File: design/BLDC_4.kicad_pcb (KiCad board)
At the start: 4 copper layers, 38.5 x 65 mm, 127 parts, among them K1 SERVO, P1 HALL/Encoder, P101 CANBUS, P2 SWD, P3 PWR_COMM, P4 IN+, P5 IN-, P6 MOTOR1, P7 MOTOR2, P9 MOTOR3, Q1 IRFS7530, Q2 IRFS7530, Q3 IRFS7530, Q4 IRFS7530, Q5 IRFS7530, Q6 IRFS7530, U1 STM32F40X_LQFP64, U2 TC2117, U3 DRV8302, U401 SN65HVD232, X1 MINI-USB-SHIELD-32005-201, X2 8MHz 10ppm

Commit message: Version 0.1 :godmode:
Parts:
- removed 1PIN (x2): P***, 1pin
- removed 1PIN (x2): P***, Connect:1pin
- removed C401, C41, C52: 2.2u, CRF1:SMD-0603_c
- removed C43, C44, C49: 10u,50V, CRF1:SMD-1206
- removed C51: 15u, 100v, w_smd_cap:c_2220
- removed G***: oshw_silkscreen-back_3mm, oshw_silkscreen-back_3mm
- removed K1: SERVO, CRF1:pinhead-1X03
- removed P101: CANBUS, JST conn:b4b-ph-kl
- removed P9: MOTOR3, CRF1:1PAD_4x5mm
- removed R103, R104: 22R, CRF1:SMD-0603_r
- removed R36, R46: 39k, CRF1:SMD-0603_r
- removed R37, R38, R48, R49, R50, R51: 100R, CRF1:SMD-0603_r
- removed R401: NI, CRF1:SMD-0603_r
- removed R402: 10k, CRF1:SMD-0603_r
- removed R42, R43: 4R7, CRF1:SMD-0603_r
- removed R53, R54: SHUNT, CRF1:WSLP2726
- removed U401: SN65HVD232, CRF1:SOIC-8-W
- removed X2: 8MHz 10ppm, CRF1:Crystal_5x3mm
- added J1: Conn_01x04, Connector_PinHeader_2.54mm:PinHeader_1x04_P2.54mm_Vertical, F.Cu at (164.5, 59.1)
- added R14: 4R7, Resistor_SMD:R_0603_1608Metric, F.Cu at (200.5, 87.0)
- added R15: 4R7, Resistor_SMD:R_0603_1608Metric, F.Cu at (200.5, 88.9)
- added R16: 39k, Resistor_SMD:R_0603_1608Metric, F.Cu at (200.7, 84.5)
- added R31: 2k2, Resistor_SMD:R_0603_1608Metric, F.Cu at (174.6, 90.2)
- C1: value 10u,50V -> 100n; footprint CRF1:SMD-1206 -> Capacitor_SMD:C_0603_1608Metric_Pad1.05x0.95mm_HandSolder
- C10, C11, C12, C23: value 2.2u -> 10u,50V; footprint CRF1:SMD-0603_c -> Capacitor_SMD:C_1206_3216Metric
- C13: value 2.2u -> 100n; footprint CRF1:SMD-0603_c -> Capacitor_SMD:C_0603_1608Metric_Pad1.05x0.95mm_HandSolder
- C14, C16: value 2.2u -> 220n; footprint CRF1:SMD-0603_c -> Capacitor_SMD:C_0603_1608Metric_Pad1.05x0.95mm_HandSolder; moved to F.Cu
- C15: value 15p -> 220n; footprint CRF1:SMD-0603_c -> Capacitor_SMD:C_0603_1608Metric_Pad1.05x0.95mm_HandSolder; moved to F.Cu
- C17, C18: value 2.2u -> 2.2n; footprint CRF1:SMD-0603_c -> Capacitor_SMD:C_0603_1608Metric_Pad1.05x0.95mm_HandSolder; moved to F.Cu
- C19: value 120p -> 2.2u; footprint CRF1:SMD-0603_c -> Capacitor_SMD:C_0603_1608Metric_Pad1.05x0.95mm_HandSolder
- C2, C3: value 100n -> 2.2u; footprint CRF1:SMD-0603_c -> Capacitor_SMD:C_0603_1608Metric_Pad1.05x0.95mm_HandSolder; moved to F.Cu
- C20: value 2.2u -> 100u; footprint CRF1:SMD-0603_c -> Capacitor_Tantalum_SMD:CP_EIA-3528-21_Kemet-B; moved to F.Cu
- C21: value 6.8n -> 10u,50V; footprint CRF1:SMD-0603_c -> Capacitor_SMD:C_1206_3216Metric
- C22: value 22n -> 100u; footprint CRF1:SMD-0603_c -> Capacitor_Tantalum_SMD:CP_EIA-3528-21_Kemet-B
- C24, C26: value 2.2u -> 10u,50V; footprint CRF1:SMD-0603_c -> Capacitor_SMD:C_1206_3216Metric; moved to F.Cu
- C25: value 100u -> 15u, 100v; footprint w_smd_cap:c_tant_B -> Capacitor_SMD:C_2220_5650Metric; moved to F.Cu
- C27: value 100n -> 10u,50V; footprint CRF1:SMD-0603_c -> Capacitor_SMD:C_1206_3216Metric
- C28: value 220n -> 15u,100V; footprint CRF1:SMD-0603_c -> Capacitor_SMD:C_2220_5650Metric
- C29: value 220n -> 15p; footprint CRF1:SMD-0603_c -> Capacitor_SMD:C_0603_1608Metric
- C30: value 220n -> 2.2u; footprint CRF1:SMD-0603_c -> Capacitor_SMD:C_0603_1608Metric
- C31: footprint CRF1:SMD-0603_c -> Capacitor_SMD:C_0603_1608Metric; moved to F.Cu
- C32: value 100n -> 2.2u; footprint CRF1:SMD-0603_c -> Capacitor_SMD:C_0603_1608Metric; moved to F.Cu
- C33: value 100u -> 100n; footprint w_smd_cap:c_tant_B -> Capacitor_SMD:C_0603_1608Metric; moved to F.Cu
- C34, C36: value 2.2n -> 2.2u; footprint CRF1:SMD-0603_c -> Capacitor_SMD:C_0603_1608Metric
- C35: value 2.2u -> 15p; footprint CRF1:SMD-0603_c -> Capacitor_SMD:C_0603_1608Metric
- C37: value 15u,100V -> 2.2u; footprint w_smd_cap:c_2220 -> Capacitor_SMD:C_0603_1608Metric
- C38: value 15p -> 2.2u; footprint CRF1:SMD-0603_c -> Capacitor_SMD:C_0603_1608Metric; moved to F.Cu
- C39: value 10u,50V -> 2.2u; footprint CRF1:SMD-1206 -> Capacitor_SMD:C_0603_1608Metric
- C4: value 4n7 -> 120p; footprint CRF1:SMD-0603_c -> Capacitor_SMD:C_0603_1608Metric_Pad1.05x0.95mm_HandSolder; moved to F.Cu
- C40: value 10u,50V -> 2.2u; footprint CRF1:SMD-1206 -> Capacitor_SMD:C_0603_1608Metric; moved to F.Cu
- C5, C6: value 4n7 -> 2.2u; footprint CRF1:SMD-0603_c -> Capacitor_SMD:C_0603_1608Metric_Pad1.05x0.95mm_HandSolder; moved to F.Cu
- C7: value 4n7 -> 6.8n; footprint CRF1:SMD-0603_c -> Capacitor_SMD:C_0603_1608Metric_Pad1.05x0.95mm_HandSolder; moved to F.Cu
- C8: value 10u,50V -> 22n; footprint CRF1:SMD-1206 -> Capacitor_SMD:C_0603_1608Metric_Pad1.05x0.95mm_HandSolder
- C9: value 10u,50V -> 2.2u; footprint CRF1:SMD-1206 -> Capacitor_SMD:C_0603_1608Metric_Pad1.05x0.95mm_HandSolder; moved to F.Cu
- D1: value GREEN -> RED; footprint LEDs:LED-0603 -> LED_SMD:LED_0603_1608Metric; moved to F.Cu
- D2: value RED -> GREEN; footprint LEDs:LED-0603 -> LED_SMD:LED_0603_1608Metric; moved to F.Cu
- D3: footprint LEDs:LED-0603 -> LED_SMD:LED_0603_1608Metric; moved to F.Cu
- D4: footprint Diodes_SMD:SMA_Handsoldering -> Diode_SMD:D_SMA_Handsoldering; moved to F.Cu
- D5: footprint w_smd_diode:do214ac -> Diode_SMD:D_SMA_Handsoldering; moved to F.Cu
- P1: value HALL/Encoder -> PWR_COMM; footprint CRF1:MICRO_JST_6 -> Connector_JST:JST_PH_B7B-PH-K_1x07_P2.00mm_Vertical
- P2: value SWD -> IN+; footprint CRF1:MICRO_JST_6 -> CRF1:1PAD_4x5mm
- P3: value PWR_COMM -> IN-; footprint CRF1:b7b-ph-kl -> CRF1:1PAD_4x5mm
- P4: value IN+ -> MOTOR3; moved to F.Cu
- P5: value IN- -> MOTOR2; moved to F.Cu
- P7: value MOTOR2 -> SWD; footprint CRF1:1PAD_4x5mm -> Connector_JST:JST_PH_B6B-PH-K_1x06_P2.00mm_Vertical
- Q1, Q3, Q5: value IRFS7530 -> Si2302CDS; footprint CRF1:D2PAK-7-GDS -> Package_TO_SOT_SMD:SOT-23
- Q2, Q4, Q6: value IRFS7530 -> Si2302CDS; footprint CRF1:D2PAK-7-GDS -> Package_TO_SOT_SMD:SOT-23; moved to F.Cu
- R1: value NTC 10k -> 39k; footprint CRF1:SMD-0603_r -> Resistor_SMD:R_0603_1608Metric
- R10, R9: value 10k -> 1mOhm; footprint CRF1:SMD-0603_r -> Resistor_SMD:R_0612_1632Metric; moved to F.Cu
- R11, R12: value 2k2 -> 4R7; footprint CRF1:SMD-0603_r -> Resistor_SMD:R_0603_1608Metric; moved to F.Cu
- R13: value 2k2 -> 39k; footprint CRF1:SMD-0603_r -> Resistor_SMD:R_0603_1608Metric; moved to F.Cu
- R17: value 18k -> 4R7; footprint CRF1:SMD-0603_r -> Resistor_SMD:R_0603_1608Metric
- R18: value 3k3 -> 4R7; footprint CRF1:SMD-0603_r -> Resistor_SMD:R_0603_1608Metric
- R19: value 15k -> 39k; footprint CRF1:SMD-0603_r -> Resistor_SMD:R_0603_1608Metric
- R2: value 10k -> 2k2; footprint CRF1:SMD-0603_r -> Resistor_SMD:R_0603_1608Metric
- R20: value 10k -> 18k; footprint CRF1:SMD-0603_r -> Resistor_SMD:R_0603_1608Metric
- R21: value 220k -> 3k3; footprint CRF1:SMD-0603_r -> Resistor_SMD:R_0603_1608Metric; moved to F.Cu
- R22: value 2k2 -> 10k; footprint CRF1:SMD-0603_r -> Resistor_SMD:R_0603_1608Metric; moved to F.Cu
- R23: value 39k -> 15k; footprint CRF1:SMD-0603_r -> Resistor_SMD:R_0603_1608Metric; moved to F.Cu
- R24: value 2k2 -> 220k; footprint CRF1:SMD-0603_r -> Resistor_SMD:R_0603_1608Metric; moved to F.Cu
- R25: footprint CRF1:SMD-0603_r -> Resistor_SMD:R_0603_1608Metric
- R26: value 39k -> 100R; footprint CRF1:SMD-0603_r -> Resistor_SMD:R_0603_1608Metric; moved to F.Cu
- R27: value 2k2 -> 100R; footprint CRF1:SMD-0603_r -> Resistor_SMD:R_0603_1608Metric; moved to F.Cu
- R28: value 4R7 -> 100R; footprint CRF1:SMD-0603_r -> Resistor_SMD:R_0603_1608Metric
- R29: value 4R7 -> 100R; footprint CRF1:SMD-0603_r -> Resistor_SMD:R_0603_1608Metric; moved to F.Cu
- R3: value 39k -> 0R; footprint CRF1:SMD-0603_r -> Resistor_SMD:R_0603_1608Metric; moved to F.Cu
- R30, R32, R33: footprint CRF1:SMD-0603_r -> Resistor_SMD:R_0603_1608Metric; moved to F.Cu
- R34: value 4R7 -> 39k; footprint CRF1:SMD-0603_r -> Resistor_SMD:R_0603_1608Metric
- R35: value 4R7 -> 2k2; footprint CRF1:SMD-0603_r -> Resistor_SMD:R_0603_1608Metric; moved to F.Cu
- R4, R5: value 2k2 -> 22R; footprint CRF1:SMD-0603_r -> Resistor_SMD:R_0603_1608Metric; moved to F.Cu
- R6: value 0R -> 100R; footprint CRF1:SMD-0603_r -> Resistor_SMD:R_0603_1608Metric; moved to F.Cu
- R7: value 10k -> 100R; footprint CRF1:SMD-0603_r -> Resistor_SMD:R_0603_1608Metric; moved to F.Cu
- R8: value 10k -> 2k2; footprint CRF1:SMD-0603_r -> Resistor_SMD:R_0603_1608Metric; moved to F.Cu
- U1: value STM32F40X_LQFP64 -> DRV8302; footprint CRF1:lqfp64_pad_mod -> Package_SO:HTSSOP-56-1EP_6.1x14mm_P0.5mm_EP3.61x6.35mm
- U2: footprint CRF1:SOT-223 -> Package_TO_SOT_SMD:SOT-223-3_TabPin2; moved to F.Cu
- U3: value DRV8302 -> STM32F40X_LQFP64; footprint CRF1:TSSOP-56-PP -> Package_QFP:LQFP-64_10x10mm_P0.5mm
- X1: value MINI-USB-SHIELD-32005-201 -> 8MHz 10ppm; footprint CRF1:USB-UX60R-MB-5ST -> Crystal:Crystal_SMD_5032-4Pin_5.0x3.2mm
- moved C25 139.3 mm to (205.1, 61.6), turned to 0 degrees
- moved C24 131.4 mm to (203.8, 66.7), turned to 0 degrees
- moved P4 131.0 mm to (208.9, 76.8)
- moved R13 130.7 mm to (204.0, 80.6), turned to 180 degrees
- moved P6 124.4 mm to (208.9, 94.6), turned to 0 degrees
- moved R11 124.2 mm to (200.0, 74.9), turned to 180 degrees
- moved R9 124.0 mm to (199.9, 78.1), turned to 180 degrees
- moved R12 123.9 mm to (199.9, 81.3), turned to 180 degrees
- moved R32 121.9 mm to (207.6, 101.0), turned to 270 degrees
- moved D4 120.7 mm to (198.8, 67.3), turned to 270 degrees
- moved Q5 119.1 mm to (203.8, 91.8), turned to 90 degrees
- moved Q6 119.0 mm to (203.8, 95.6), turned to 90 degrees
- moved R17 116.4 mm to (200.2, 92.7), turned to 180 degrees
- moved L1 114.6 mm to (193.0, 67.3), turned to 90 degrees
- moved R10 114.4 mm to (200.1, 95.9), turned to 180 degrees
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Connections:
- C1 pad 2: V_SUPPLY -> /MCU/AN_IN
- C10 pad 1: GND -> V_SUPPLY
- C10 pad 2: VCC -> GND
- C11 pad 1: GND -> V_SUPPLY
- C11 pad 2: VCC -> GND
- C12 pad 1: GND -> V_SUPPLY
- C12 pad 2: VCC -> GND
- C13 pad 1: GND -> Net-(C13-Pad1)
- C13 pad 2: VCC -> Net-(C13-Pad2)
- C14 pad 1: GND -> /Mosfet driver/H1_VS
- C14 pad 2: VCC -> Net-(C14-Pad2)
- C15 pad 1: Net-(C15-Pad1) -> /Mosfet driver/H2_VS
- C15 pad 2: GND -> Net-(C15-Pad2)
- C16 pad 1: Net-(C16-Pad1) -> /Mosfet driver/H3_VS
- C16 pad 2: GND -> Net-(C16-Pad2)
- C17 pad 2: GND -> Net-(C17-Pad2)
- C18 pad 2: GND -> Net-(C18-Pad2)
- C19 pad 1: GND -> VCC
- C19 pad 2: Net-(C19-Pad2) -> GND
- C2 pad 1: GND -> Net-(C2-Pad1)
- C2 pad 2: /MCU/AN_IN -> GND
- C20 pad 1: GND -> VCC
- C20 pad 2: Net-(C20-Pad2) -> GND
- C21 pad 2: Net-(C21-Pad2) -> V_SUPPLY
- C22 pad 1: Net-(C22-Pad1) -> +5V
- C22 pad 2: Net-(C22-Pad2) -> GND
- C23 pad 2: Net-(C23-Pad2) -> V_SUPPLY
- C24 pad 1: VCC -> GND
- C24 pad 2: GND -> V_SUPPLY
- C25 pad 1: VCC -> GND
- C25 pad 2: GND -> V_SUPPLY
- C26 pad 1: Net-(C18-Pad1) -> GND
- C26 pad 2: GND -> V_SUPPLY
- C27 pad 1: Net-(C27-Pad1) -> GND
- C27 pad 2: Net-(C27-Pad2) -> V_SUPPLY
- C28 pad 1: /Mosfet driver/H1_VS -> GND
- C28 pad 2: Net-(C28-Pad2) -> V_SUPPLY
- C29 pad 1: /Mosfet driver/H2_VS -> Net-(C29-Pad1)
- C29 pad 2: Net-(C29-Pad2) -> GND
- C3 pad 1: GND -> Net-(C2-Pad1)
- C3 pad 2: /MCU/SERVO -> GND
- C30 pad 1: /Mosfet driver/H3_VS -> Net-(C30-Pad1)
- C30 pad 2: Net-(C30-Pad2) -> GND
- C31 pad 1: GND -> Net-(C31-Pad1)
- C31 pad 2: VCC -> GND
- C32 pad 2: NRST -> VCC
- C33 pad 1: +5V -> GND
- C33 pad 2: GND -> NRST
- C34 pad 1: Net-(C34-Pad1) -> GND
- C34 pad 2: Net-(C34-Pad2) -> VCC
- C35 pad 1: GND -> Net-(C35-Pad1)
- C35 pad 2: VCC -> GND
- C36 pad 1: Net-(C36-Pad1) -> GND
- C36 pad 2: Net-(C36-Pad2) -> VCC
- C37 pad 2: V_SUPPLY -> VCC
- C38 pad 1: Net-(C38-Pad1) -> GND
- C38 pad 2: GND -> VCC
- C39 pad 2: V_SUPPLY -> VCC
- C4 pad 2: /Filters/TEMP_IN -> Net-(C4-Pad2)
- C40 pad 2: V_SUPPLY -> VCC
- C5 pad 1: /Filters/HALL3_OUT -> GND
- C5 pad 2: GND -> Net-(C5-Pad2)
- C6 pad 1: /Filters/HALL2_OUT -> GND
- C6 pad 2: GND -> Net-(C5-Pad2)
- C7 pad 1: /Filters/HALL1_OUT -> GND
- C7 pad 2: GND -> Net-(C7-Pad2)
- C8 pad 1: GND -> Net-(C8-Pad1)
- C8 pad 2: V_SUPPLY -> Net-(C8-Pad2)
- C9 pad 2: V_SUPPLY -> Net-(C9-Pad2)
- D4 pad 2: Net-(C27-Pad1) -> Net-(C13-Pad1)
- D5 pad 1: GND -> +5V
- D5 pad 2: +5V -> GND
- L1 pad 1: Net-(C27-Pad1) -> Net-(C13-Pad1)
- P1 pad 2: /Filters/TEMP_IN -> VCC
- P1 pad 3: /Filters/HALL1_IN -> GND
- P1 pad 4: /Filters/HALL2_IN -> /SCK_ADC_EXT
- P1 pad 5: /Filters/HALL3_IN -> /TX_SDA
- P1 pad 6: GND -> /RX_SCL_MOSI
- P2 pad 1: VCC -> V_SUPPLY
- P3 pad 1: +5V -> GND
- P4 pad 1: V_SUPPLY -> /Mosfet driver/H1_VS
- P5 pad 1: GND -> /Mosfet driver/H2_VS
- P7 pad 1: /Mosfet driver/H2_VS -> VCC
- R1 pad 1: VCC -> V_SUPPLY
- R1 pad 2: /MCU/ADC_TEMP -> /MCU/AN_IN
- R10 pad 1: /Filters/HALL3_IN -> /Mosfet driver/H3_LOW
- R10 pad 2: /Filters/HALL3_OUT -> GND
- R11 pad 1: /Filters/HALL3_IN -> Net-(Q1-Pad1)
- R11 pad 2: VCC -> /Mosfet driver/M_H1
- R12 pad 1: /Filters/HALL2_IN -> Net-(Q2-Pad1)
- R12 pad 2: VCC -> /Mosfet driver/M_L1
- R13 pad 1: /Filters/HALL1_IN -> /Mosfet driver/H1_LOW
- R13 pad 2: VCC -> Net-(Q2-Pad1)
- R17 pad 1: +5V -> Net-(Q5-Pad1)
- R17 pad 2: Net-(R17-Pad2) -> /Mosfet driver/M_H3
- R18 pad 1: Net-(R17-Pad2) -> Net-(Q6-Pad1)
- R18 pad 2: GND -> /Mosfet driver/M_L3
- R19 pad 1: Net-(C21-Pad2) -> /Mosfet driver/H3_LOW
- R19 pad 2: Net-(C19-Pad2) -> Net-(Q6-Pad1)
- R2 pad 1: /MCU/ADC_TEMP -> GND
- R2 pad 2: GND -> /MCU/AN_IN
- R20 pad 1: Net-(R20-Pad1) -> +5V
- R20 pad 2: GND -> Net-(R20-Pad2)
- R21 pad 1: GND -> Net-(R20-Pad2)
- R21 pad 2: Net-(R21-Pad2) -> GND
- R22 pad 1: Net-(D3-Pad1) -> Net-(R22-Pad1)
- R22 pad 2: VCC -> GND
- R23 pad 1: /Mosfet driver/H3_VS -> Net-(C7-Pad2)
- R23 pad 2: /MCU/SENS1 -> Net-(C4-Pad2)
- R24 pad 2: /MCU/SENS1 -> Net-(R24-Pad2)
- R26 pad 1: /Mosfet driver/H2_VS -> /Mosfet driver/H3_LOW
- R26 pad 2: /MCU/SENS2 -> Net-(C17-Pad1)
- R27 pad 2: /MCU/SENS2 -> Net-(C17-Pad2)
- R28 pad 1: Net-(Q1-PadG) -> /Mosfet driver/H1_LOW
- R28 pad 2: /Mosfet driver/M_H1 -> Net-(C18-Pad1)
- R29 pad 1: Net-(Q2-PadG) -> GND
- R29 pad 2: /Mosfet driver/M_L1 -> Net-(C18-Pad2)
- R3 pad 1: V_SUPPLY -> Net-(J1-Pad1)
- R3 pad 2: /MCU/AN_IN -> +5V
- R30 pad 1: /Mosfet driver/H1_LOW -> /Mosfet driver/H3_VS
- R30 pad 2: Net-(Q2-PadG) -> /MCU/SENS1
- R32 pad 1: /Mosfet driver/H1_VS -> /Mosfet driver/H2_VS
- R32 pad 2: /MCU/SENS3 -> /MCU/SENS2
- R33 pad 2: /MCU/SENS3 -> /MCU/SENS2
- R34 pad 1: Net-(Q3-PadG) -> /Mosfet driver/H1_VS
- R34 pad 2: /Mosfet driver/M_H2 -> /MCU/SENS3
- R35 pad 1: Net-(Q4-PadG) -> GND
- R35 pad 2: /Mosfet driver/M_L2 -> /MCU/SENS3
- R4 pad 1: GND -> /MCU/USB_DM
- R4 pad 2: /MCU/AN_IN -> Net-(J1-Pad2)
- R5 pad 1: /MCU/SERVO -> /MCU/USB_DP
- R6 pad 1: Net-(R6-Pad1) -> Net-(D1-Pad1)
- R6 pad 2: +5V -> /MCU/LED_RED
- R7 pad 1: /Filters/TEMP_IN -> Net-(D2-Pad1)
- R7 pad 2: VCC -> /MCU/LED_GREEN
- R8 pad 1: /Filters/HALL1_IN -> Net-(D3-Pad1)
- R8 pad 2: /Filters/HALL1_OUT -> VCC
- R9 pad 1: /Filters/HALL2_IN -> /Mosfet driver/H1_LOW
- R9 pad 2: /Filters/HALL2_OUT -> GND
- U1 pad 1: VCC -> Net-(R24-Pad2)
- U1 pad 10: /MCU/AN_IN -> GND
- U1 pad 11: Net-(U1-Pad11) -> Net-(C5-Pad2)
- U1 pad 12: GND -> /MCU/DC_CAL
- U1 pad 13: VCC -> Net-(C2-Pad1)
- U1 pad 14: /MCU/SENS3 -> Net-(C8-Pad1)
- U1 pad 15: /MCU/SENS2 -> Net-(C8-Pad2)
- U1 pad 16: /MCU/SENS1 -> /MCU/EN_GATE
- U1 pad 17: /MCU/ADC_TEMP -> /MCU/H1
- U1 pad 18: GND -> /MCU/L1
- U1 pad 19: VCC -> /MCU/H2
- U1 pad 2: Net-(U1-Pad2) -> Net-(C4-Pad2)
- U1 pad 20: /MCU/TX_SDA_NSS -> /MCU/L2
- U1 pad 21: /MCU/SCK_ADC_EXT -> /MCU/H3
- U1 pad 22: /MCU/MISO_ADC_EXT2 -> /MCU/L3
- U1 pad 23: /MCU/RX_SCL_MOSI -> Net-(C5-Pad2)
- U1 pad 24: /MCU/LED_GREEN -> VCC
- U1 pad 25: /MCU/LED_RED -> /MCU/BR_SO1
- U1 pad 27: /MCU/BR_SO1 -> Net-(C9-Pad2)
- U1 pad 28: Net-(U1-Pad28) -> GND
- U1 pad 29: /MCU/RX_SCL_MOSI -> V_SUPPLY
- U1 pad 3: Net-(U1-Pad3) -> Net-(R20-Pad2)
- U1 pad 30: /MCU/TX_SDA_NSS -> Net-(C18-Pad2)
- U1 pad 31: Net-(C16-Pad1) -> Net-(C18-Pad1)
- U1 pad 32: VCC -> Net-(C17-Pad2)
- U1 pad 33: /MCU/DC_CAL -> Net-(C17-Pad1)
- U1 pad 34: /MCU/L3 -> /Mosfet driver/H3_LOW
- U1 pad 35: /MCU/L2 -> /Mosfet driver/M_L3
- U1 pad 36: /MCU/L1 -> /Mosfet driver/H3_VS
- U1 pad 37: /MCU/TX_SDA_NSS -> /Mosfet driver/M_H3
- U1 pad 38: /MCU/RX_SCL_MOSI -> Net-(C16-Pad2)
- U1 pad 39: Net-(U1-Pad39) -> GND
- U1 pad 40: Net-(U1-Pad40) -> /Mosfet driver/M_L2
- U1 pad 41: /MCU/H3 -> /Mosfet driver/H2_VS
- U1 pad 42: /MCU/H2 -> /Mosfet driver/M_H2
- U1 pad 43: /MCU/H1 -> Net-(C15-Pad2)
- U1 pad 44: /MCU/USB_DM -> /Mosfet driver/H1_LOW
- U1 pad 45: /MCU/USB_DP -> /Mosfet driver/M_L1
- U1 pad 46: SWDIO -> /Mosfet driver/H1_VS
- U1 pad 47: Net-(C17-Pad1) -> /Mosfet driver/M_H1
- U1 pad 48: VCC -> Net-(C14-Pad2)
- U1 pad 49: SWCLK -> Net-(R25-Pad2)
- U1 pad 5: Net-(C15-Pad1) -> Net-(U1-Pad5)
- U1 pad 50: Net-(U1-Pad50) -> Net-(C13-Pad1)
- U1 pad 51: /MCU/EN_GATE -> Net-(C13-Pad1)
- U1 pad 52: /Filters/HALL3_OUT -> Net-(C13-Pad2)
- U1 pad 53: /MCU/FAULT -> V_SUPPLY
- U1 pad 54: Net-(U1-Pad54) -> V_SUPPLY
- U1 pad 57: /MCU/SERVO -> GND
- U1 pad 6: Net-(C38-Pad1) -> /MCU/FAULT
- U1 pad 7: NRST -> Net-(R22-Pad1)
- U1 pad 8: /Filters/TEMP_IN -> GND
- U1 pad 9: Net-(U1-Pad9) -> VCC
- U3 pad 1: Net-(R21-Pad2) -> VCC
- U3 pad 10: GND -> /MCU/AN_IN
- U3 pad 11: Net-(C20-Pad2) -> Net-(U3-Pad11)
- U3 pad 12: /MCU/DC_CAL -> GND
- U3 pad 13: Net-(C18-Pad1) -> VCC
- U3 pad 14: Net-(C22-Pad1) -> /MCU/SENS3
- U3 pad 15: Net-(C22-Pad2) -> /MCU/SENS2
- U3 pad 16: /MCU/EN_GATE -> /MCU/SENS1
- U3 pad 17: /MCU/H1 -> /MCU/ADC_TEMP
- U3 pad 18: /MCU/L1 -> GND
- U3 pad 19: /MCU/H2 -> VCC
- U3 pad 2: Net-(C19-Pad2) -> Net-(U3-Pad2)
- U3 pad 20: /MCU/L2 -> /TX_SDA
- U3 pad 21: /MCU/H3 -> /SCK_ADC_EXT
- U3 pad 22: /MCU/L3 -> /MISO_RX_SCL
- U3 pad 23: Net-(C20-Pad2) -> /RX_SCL_MOSI
- U3 pad 24: VCC -> /MCU/LED_GREEN
- U3 pad 25: /MCU/BR_SO1 -> /MCU/LED_RED
- U3 pad 27: Net-(C23-Pad2) -> /MCU/BR_SO1
- U3 pad 28: GND -> Net-(U3-Pad28)
- U3 pad 29: V_SUPPLY -> /RX_SCL_MOSI
- U3 pad 3: Net-(R17-Pad2) -> Net-(U3-Pad3)
- U3 pad 30: Net-(C36-Pad2) -> /TX_SDA
- U3 pad 31: Net-(C36-Pad1) -> Net-(C30-Pad1)
- U3 pad 32: Net-(C34-Pad2) -> VCC
- U3 pad 33: Net-(C34-Pad1) -> /MCU/DC_CAL
- U3 pad 34: /Mosfet driver/H3_LOW -> /MCU/L3
- U3 pad 35: /Mosfet driver/M_L3 -> /MCU/L2
- U3 pad 36: /Mosfet driver/H3_VS -> /MCU/L1
- U3 pad 37: /Mosfet driver/M_H3 -> /TX_SDA
- U3 pad 38: Net-(C30-Pad2) -> /RX_SCL_MOSI
- U3 pad 39: GND -> Net-(U3-Pad39)
- U3 pad 40: /Mosfet driver/M_L2 -> Net-(U3-Pad40)
- U3 pad 41: /Mosfet driver/H2_VS -> /MCU/H3
- U3 pad 42: /Mosfet driver/M_H2 -> /MCU/H2
- U3 pad 43: Net-(C29-Pad2) -> /MCU/H1
- U3 pad 44: /Mosfet driver/H1_LOW -> /MCU/USB_DM
- U3 pad 45: /Mosfet driver/M_L1 -> /MCU/USB_DP
- U3 pad 46: /Mosfet driver/H1_VS -> SWDIO
- U3 pad 47: /Mosfet driver/M_H1 -> Net-(C31-Pad1)
- U3 pad 48: Net-(C28-Pad2) -> VCC
- U3 pad 49: Net-(R25-Pad2) -> SWCLK
- U3 pad 5: Net-(U3-Pad5) -> Net-(C29-Pad1)
- U3 pad 50: Net-(C27-Pad1) -> Net-(U3-Pad50)
- U3 pad 51: Net-(C27-Pad1) -> /MCU/EN_GATE
- U3 pad 52: Net-(C27-Pad2) -> Net-(U3-Pad52)
- U3 pad 53: V_SUPPLY -> /MCU/FAULT
- U3 pad 54: V_SUPPLY -> Net-(U3-Pad54)
- U3 pad 57: GND -> Net-(U3-Pad57)
- U3 pad 6: /MCU/FAULT -> Net-(C35-Pad1)
- U3 pad 7: Net-(R20-Pad1) -> NRST
- U3 pad 8: GND -> Net-(U3-Pad8)
- U3 pad 9: VCC -> Net-(U3-Pad9)
- X1 pad 1: Net-(R6-Pad1) -> Net-(C29-Pad1)
- X1 pad 2: Net-(R103-Pad2) -> Net-(C35-Pad1)
- X1 pad 3: Net-(R104-Pad2) -> GND
- X1 pad 4: Net-(X1-Pad4) -> (no net)
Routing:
- net GND: track 398.8 -> 31.9 mm, vias 27 -> 4
- net V_SUPPLY: track 290.3 -> 85.7 mm, vias 20 -> 16
- net /Mosfet driver/H3_VS: track 166.9 -> 45.9 mm, vias 18 -> 0
- net VCC: track 185.2 -> 80.1 mm, vias 9 -> 11
- net /Mosfet driver/H1_VS: track 150.6 -> 52.9 mm, vias 17 -> 2
- net /Mosfet driver/H2_VS: track 145.0 -> 50.7 mm, vias 17 -> 2
- net /TX_SDA: track 0.00 -> 51.5 mm, vias 0 -> 5
- net /MCU/SENS1: track 26.3 -> 75.2 mm
- net /MCU/TX_SDA_NSS: track 47.1 -> 0.00 mm, vias 2 -> 0
- net /MCU/SENS2: track 28.6 -> 73.7 mm
- net /MCU/ADC_TEMP: track 44.0 -> 0.00 mm
- net /MCU/SENS3: track 30.2 -> 72.5 mm
- net /RX_SCL_MOSI: track 0.00 -> 42.2 mm, vias 0 -> 6
- net /MCU/RX_SCL_MOSI: track 41.6 -> 0.00 mm, vias 1 -> 0
- net /MCU/MISO_ADC_EXT2: track 36.0 -> 0.00 mm, vias 1 -> 0
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- added copper zone on F.Cu, net Net-(C13-Pad1)
- added copper zone on B.Cu, net V_SUPPLY
- removed copper zone on B.Cu, net /Mosfet driver/H1_LOW
- removed copper zone on B.Cu, net /Mosfet driver/H1_VS
- removed copper zone on F.Cu, net /Mosfet driver/H1_VS
- removed copper zone on GND, net /Mosfet driver/H1_VS
- removed copper zone on GND2, net /Mosfet driver/H1_VS
- removed copper zone on B.Cu, net /Mosfet driver/H2_VS
- removed copper zone on F.Cu, net /Mosfet driver/H2_VS
- removed copper zone on GND, net /Mosfet driver/H2_VS
- removed copper zone on GND2, net /Mosfet driver/H2_VS
- removed copper zone on B.Cu, net /Mosfet driver/H3_LOW
- removed copper zone on B.Cu, net /Mosfet driver/H3_VS
- removed copper zone on F.Cu, net /Mosfet driver/H3_VS
- removed copper zone on GND, net /Mosfet driver/H3_VS
- removed copper zone on GND2, net /Mosfet driver/H3_VS
- removed copper zone on B.Cu, net GND
- removed copper zone on GND, net GND
- removed copper zone on GND2, net GND
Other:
- board size 38.5 x 65 mm -> 80 x 48.9 mm
- copper layers 4 -> 2
- net class Default: clearance 0.1778 -> 0.127; trace_width 0.2032 -> 0.127; via_dia 0.8 -> 0.6; via_drill 0.5 -> 0.3
- rule trace_clearance: 0.1778 -> 0.127
- rule trace_min: 0.2032 -> 0.127
- rule via_min_drill: 0.5 -> 0.3
- rule via_min_size: 0.8 -> 0.6
- board text added: "BAT+"
- board text removed: "3.3V"
- board text removed: "3.3v"
- board text removed: "5v"
- board text removed: "ADC"
- board text removed: "ADC2"
- board text removed: "Benjamin Vedder"
- board text removed: "CANH"
- board text removed: "CANL"
- board text removed: "CLK"
- board text removed: "DIO"
- board text removed: "H1"
- board text removed: "H2"
- board text removed: "H3"
- board text removed: "MISO"
- board text removed: "MOSI"
- board text removed: "NSS"
- board text removed: "RST"
- board text removed: "RX"
- board text removed: "SCK"
- board text removed: "SCL"
- board text removed: "SDA"
- board text removed: "TEMP"
- board text removed: "TX"
- board text removed: "VESC 4.12"
- board text removed: "vedder.se"

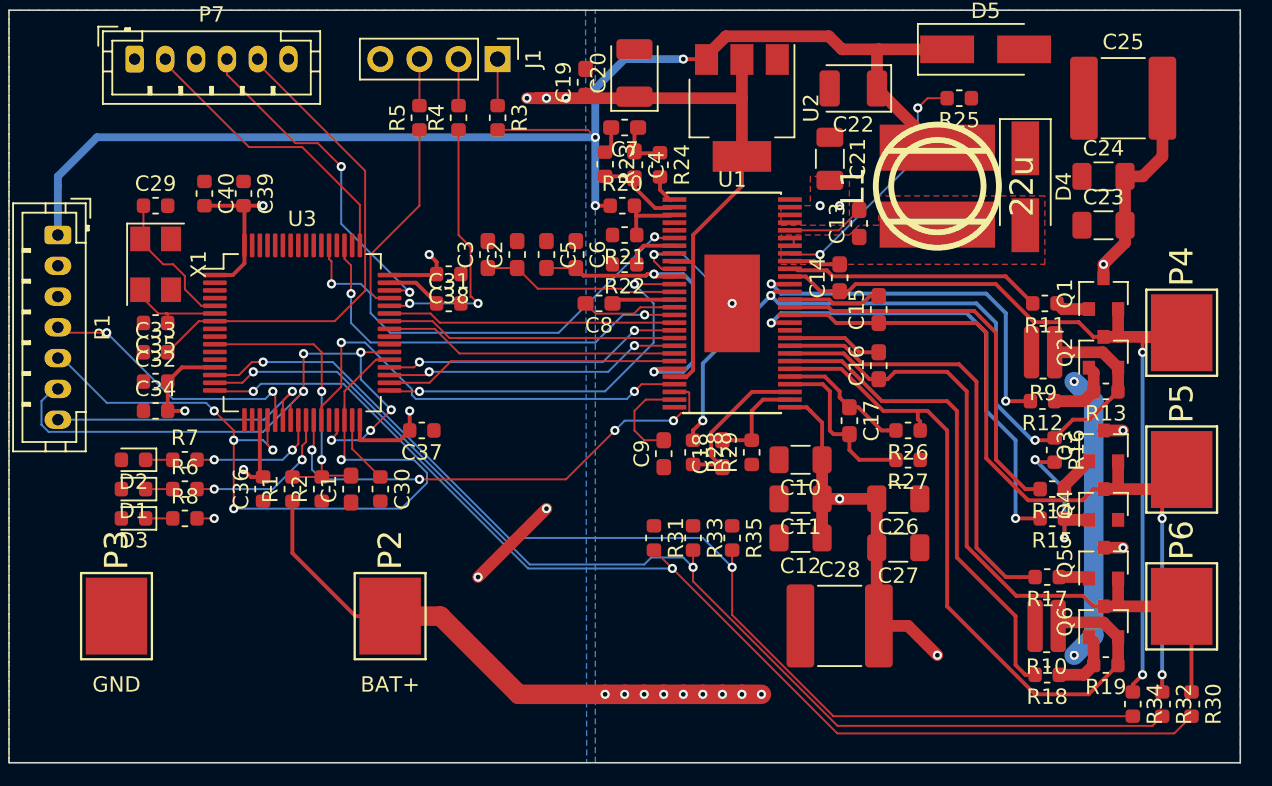
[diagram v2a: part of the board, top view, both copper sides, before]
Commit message: Nailing down the connecting pads with vias and Connecting the Filter Caps better
Turns out you CAN put lipstick on a pig :+1:
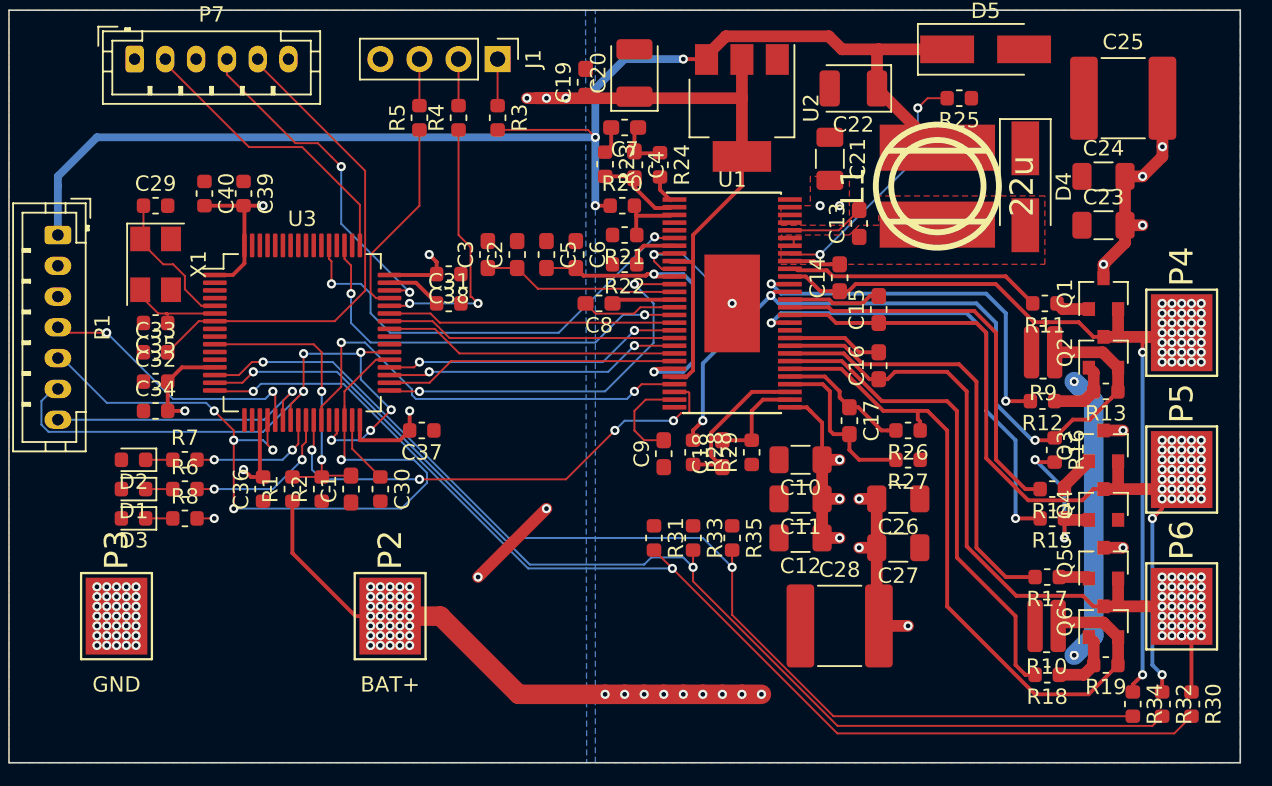
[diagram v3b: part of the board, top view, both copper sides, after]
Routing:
- net /Mosfet driver/H3_VS: track 45.9 -> 44.6 mm, vias 0 -> 36
- net /Mosfet driver/H1_VS: track 52.9 -> 51.7 mm, vias 2 -> 37
- net V_SUPPLY: track 85.7 -> 86.3 mm, vias 16 -> 58
- net /Mosfet driver/H2_VS: track 50.7 -> 51.3 mm, vias 2 -> 37
- net GND: vias 4 -> 39

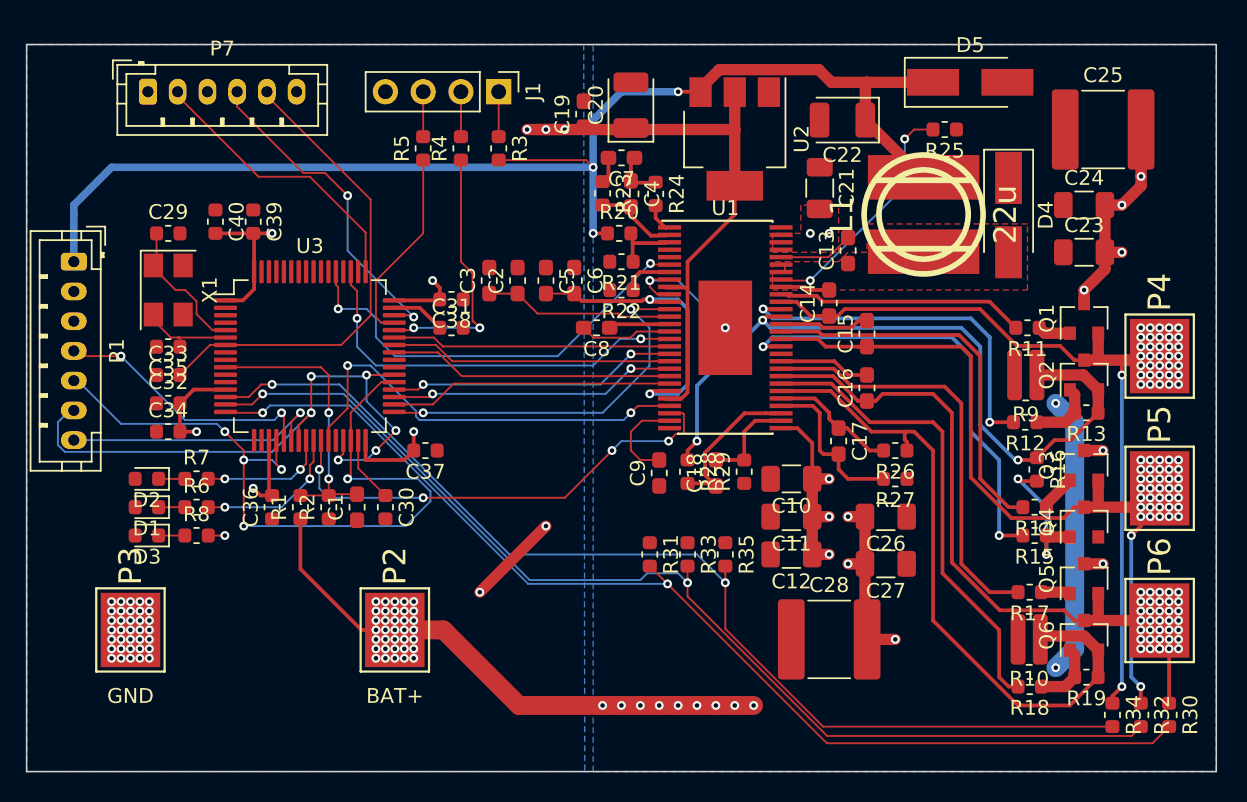
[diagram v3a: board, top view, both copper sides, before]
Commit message: Reworked Silkscreen :suspect:
It no longer looks like a pile of :shit:
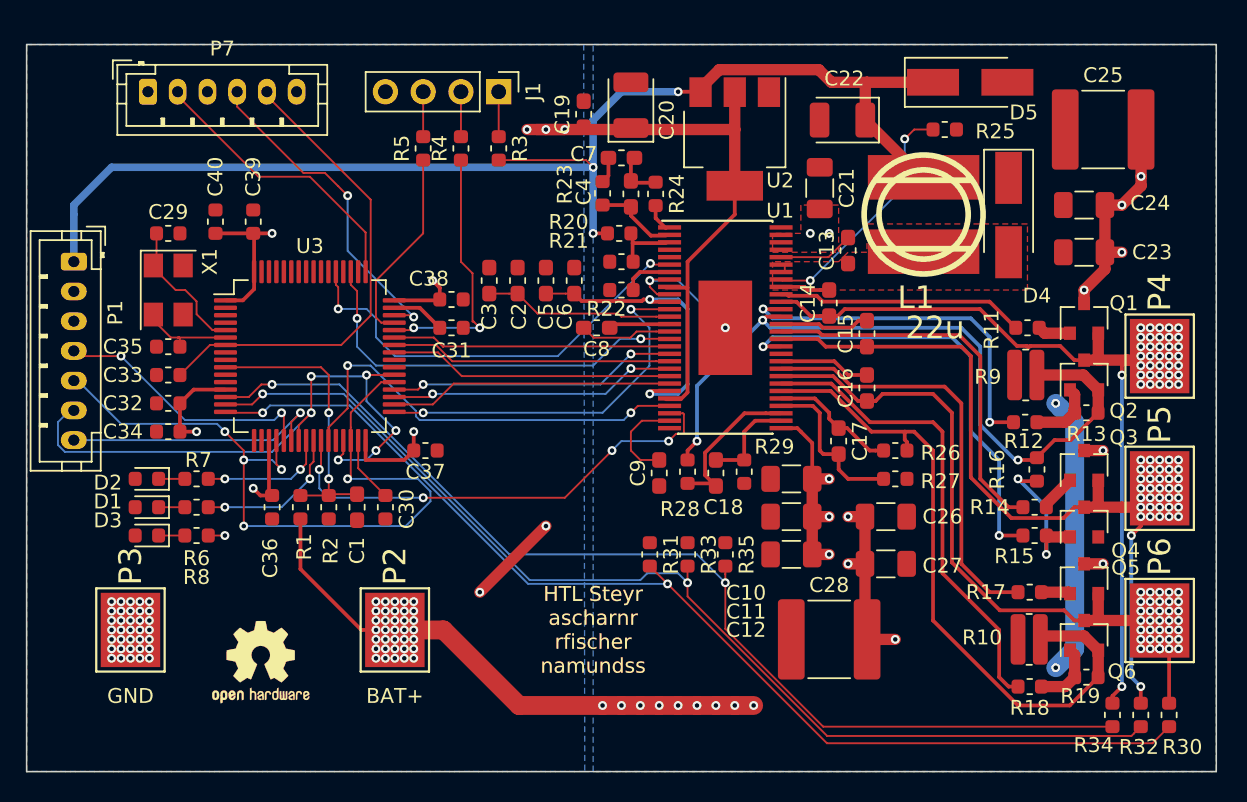
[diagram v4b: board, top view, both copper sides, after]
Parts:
- added REF**: OSHW-Logo2_7.3x6mm_SilkScreen, Symbol:OSHW-Logo2_7.3x6mm_SilkScreen, F.Cu at (148.5, 97.4)
- added REF**: OSHW-Logo2_7.3x6mm_Copper, Symbol:OSHW-Logo2_7.3x6mm_Copper, F.Cu at (148.5, 97.4)
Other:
- board text added: "HTL Steyr ascharnr rfischer namundss"
